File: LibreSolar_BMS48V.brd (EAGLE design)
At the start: 100 x 80 mm, 185 parts, among them IC1 BQ76940, Q1 ZXMP10A13F, Q10 DMN2004K, Q11 DMN2004K, Q12 DMN2004K, Q13 DMN2004K, Q14 DMN2004K, Q15 DMN2004K, Q16 DMN2004K, Q17 DMN2004K, Q18 DMN2004K, Q19 DMN2004K, Q2 FDMT80080DC, Q3 FDMT80080DC, Q4 2N7002ET1G, Q5 DMN2004K, Q6 DMN2004K, Q7 DMN2004K, Q8 DMN2004K, Q9 DMN2004K, U1 BQ76200, U2 LMR16006X, U3 ATMEGA328, Y1 8MHz

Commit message: Pinout of extension connector (LSX) changed
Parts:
- C10: value 4.7µ -> 1µ
- C19: value 470n -> 1µ
- LMX1: device resolut:LIBRE-CONNECTOR-10-2 -> LibreSolar:LIBRE-STD-EXT_SMALL
- R10: value 5m -> 1m
- moved LMX1 28.0 mm to (89.0, 48.0)
- moved N1 12.0 mm to (69.0, 40.0)
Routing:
- net D9: track 15.9 -> 44.4 mm
- net A0: track 50.8 -> 78.8 mm
- net A2: track 37.4 -> 65.4 mm
- net A1: track 27.8 -> 55.8 mm
- net D5: track 18.7 -> 46.7 mm
- net D3: track 33.9 -> 61.9 mm
- net SCL: track 61.6 -> 89.6 mm
- net SCK: track 68.2 -> 96.2 mm
- net SDA: track 67.7 -> 95.7 mm
- net 3.3V: track 172.8 -> 200.6 mm, vias 3 -> 4
- net SS: track 25.4 -> 52.0 mm
- net MOSI: track 40.8 -> 66.7 mm, vias 1 -> 2
- net RX: track 60.5 -> 85.8 mm
- net MISO: track 45.4 -> 68.6 mm, vias 1 -> 2
- net TX: track 66.4 -> 85.8 mm, vias 2 -> 3
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
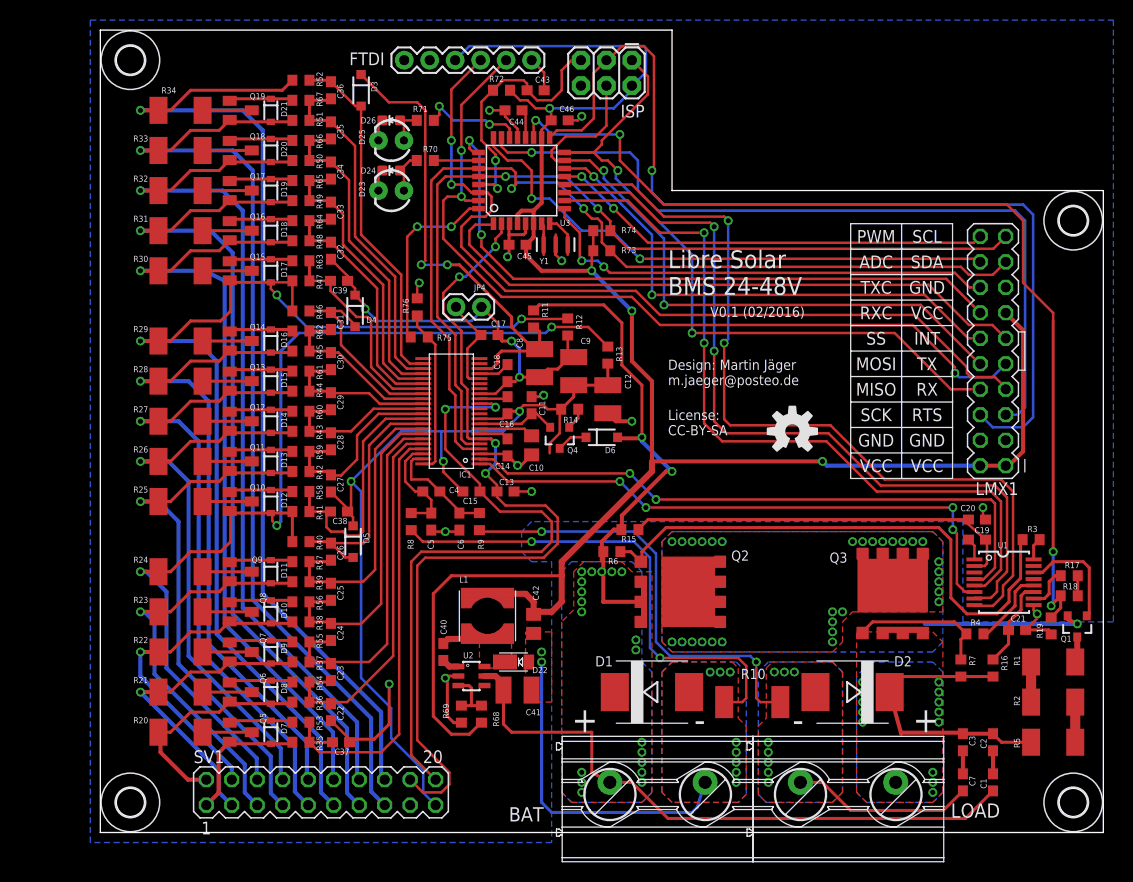
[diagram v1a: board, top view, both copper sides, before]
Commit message: Complete redesign with STM32F072 and external power part
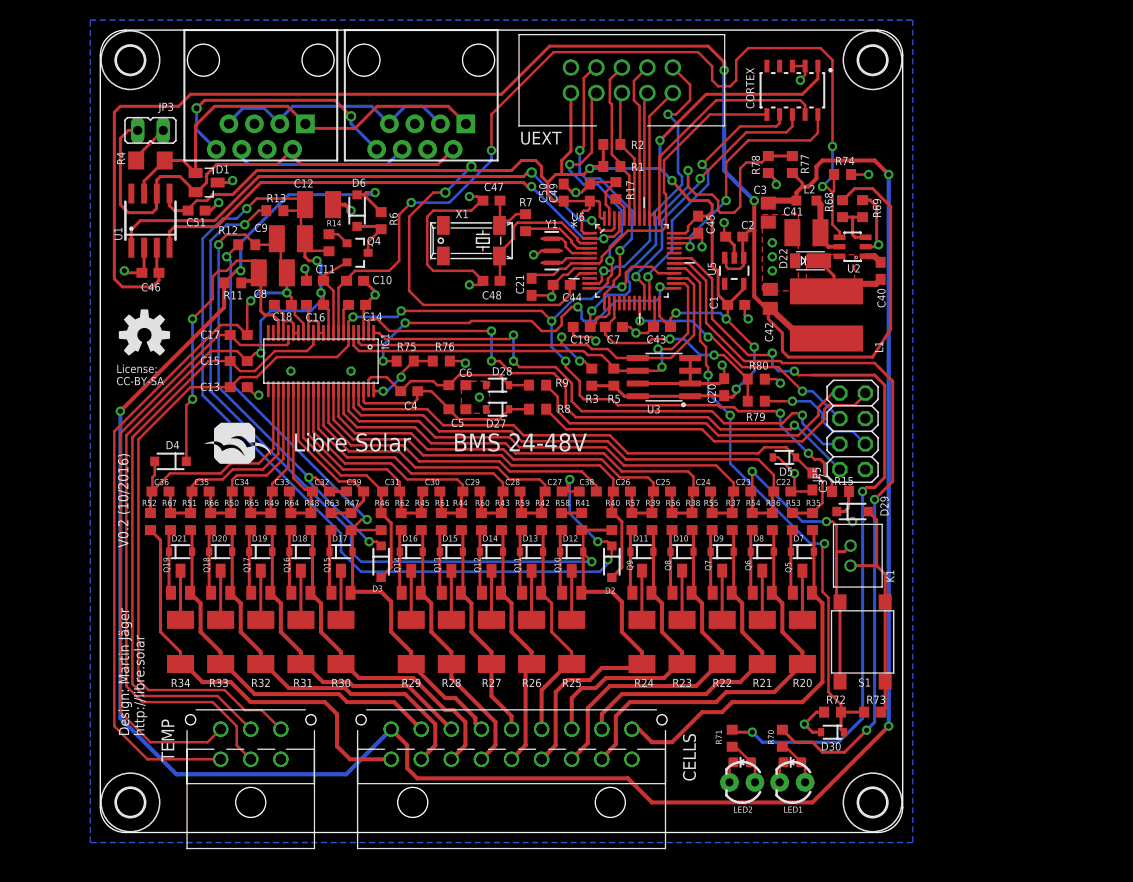
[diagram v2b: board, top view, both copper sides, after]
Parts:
- removed BAT, LOAD: MKDS_5/2-9,52, resolut:MKDS_5/2-952
- removed D23, D25: (no value), SparkFun-LED:LED3MM
- removed FTDI: FTDI Basic, SparkFun:1X06
- removed ISP: AVR_SPI_PRG_6PTH, SparkFun-Connectors:2X3
- removed JP4: M02PTH, SparkFun-Connectors:1X02
- removed LMX1: (no value), LibreSolar:LIBRE-STD-EXT_SMALL
- removed Q1: ZXMP10A13F, SparkFun-DiscreteSemi:SOT23-3
- removed Q2, Q3: FDMT80080DC, resolut:FDMT80080DC
- removed R10: 1m, rcl:R2512
- removed R16: 100, rcl:R0603
- removed R18: 100k, rcl:R0603
- removed R19: 10k, rcl:R0603
- removed SV1: (no value), con-lstb:MA10-2
- added C47, C48: 12.5p, rcl:C0603
- added C49, C51: 100n, rcl:C0603
- added C50: 2.2µ, rcl:C0603
- added CELLS: (no value), Wire_to_Board_Connectors_rev15d:66201821022
- added CORTEX: CORTEX_DEBUGSMD, LibreSolar:SAMTECH_FTSH-105-01
- added D27, D28, D30: 3.3V, SparkFun-DiscreteSemi:SOD-323
- added D29: 1N4148W, SparkFun-DiscreteSemi:SOD-123
- added JP1, JP2: RJ45, SparkFun-Connectors:RJ45-8
- added JP3: (no value), jumper:JP1
- added JP5: (no value), pinhead:2X04
- added K1: 62000211622, Wire_to_Board_Connectors_rev15d:62000211622
- added K4: 66200621122, Wire_to_Board_Connectors_rev15d:66200621122
- added K5: 66201821122, Wire_to_Board_Connectors_rev15d:66201821122
- added L2: 4.7uH, rcl:L2012C
- added LED1, LED2: (no value), SparkFun-LED:LED3MM
- added R77, R79: 100k, rcl:R0603
- added R78, R80: 5.6k, rcl:R0603
- added S1: (no value), EAGLE-TACT_SWITCHES-rev16e:430182050816
- added TEMP: 66200621022, Wire_to_Board_Connectors_rev15d:66200621022
- added U$1: LIBRESOLAR_LOGO, LibreSolar:LIBRESOLAR_LOGO
- added U5: MIC5225, SparkFun-PowerIC:SOT23-5
- added U6: STM32F072CB, LibreSolar:QFP50P900X900X160-48N
- added UEXT: UEXT, LibreSolar:UEXT
- added X1: ABS25-32.768KHZ-T, crystal:MM20SS
- C1: value 100n -> 2.2µ
- C10: device rcl:C0805 -> rcl:C0603
- C13, C15, C17: value 100n -> 4.7n
- C19: value 1µ -> 100n
- C2: value 100n -> 1µ
- C20, C21: value 10n -> 100n
- C3: value 100n -> 1µ; device rcl:C0603 -> rcl:C0805
- D1: value SMCJ75A -> PESD2CAN; device diode:SMC -> LibreSolar:SOT23
- D2: value ES3D-E3/57T -> 1N4148W; device diode:SMC -> SparkFun-DiscreteSemi:SOD-123
- D5: value 1N4148W -> 3.3V; device SparkFun-DiscreteSemi:SOD-123 -> SparkFun-DiscreteSemi:SOD-323
- IC1: device resolut:TSSOP44 -> LibreSolar:TSSOP44
- L1: value 100uH -> 47uH; device PowerMagnetics:WE-TPC_4818/4828 -> PowerMagnetics:WE-TPC_6823
- Q4: value 2N7002ET1G -> BSS123
- R1, R2, R5: value 33 -> 2.2k; device rcl:R2010 -> rcl:R0603
- R15: value 100 -> 5.6k
- R17: value 100k -> 10k
- R3: value 5 -> 2.2k
- R4: value 5 -> 120; device rcl:R0603 -> rcl:R1206
- R6: value 1M -> t.b.d.
- R68: value 33k -> 56k
- R7: value 1M -> 0R
- R72: value 10k -> 100k
- R73: value 2.2k -> 10k
- R74: value 2.2k -> 100k
- U1: value BQ76200 -> TJA1042T/3; device resolut:TSSOP16 -> LibreSolar:SOIC-8-N
- U3: value ATMEGA328 -> M24256-BW; device SparkFun:TQFP32-08 -> SparkFun-DigitalIC:SO08
- moved R4 94.8 mm to (5.00, 67.0)
- moved U1 92.3 mm to (5.00, 61.0), turned to 0 degrees
- moved D26 72.9 mm to (64.0, 7.00)
- moved D24 71.3 mm to (69.0, 7.00)
- moved R2 70.9 mm to (51.0, 68.6), turned to 180 degrees
- moved R72 70.2 mm to (73.0, 12.0)
- moved R71 68.8 mm to (63.0, 9.40), turned to 90 degrees
- moved R70 67.7 mm to (68.0, 9.40), turned to 90 degrees
- moved D1 67.5 mm to (10.6, 64.8), turned to 270 degrees
- moved R1 66.2 mm to (51.0, 66.4)
- moved N1 65.3 mm to (4.40, 49.6)
- moved R69 64.3 mm to (76.0, 62.2), turned to 270 degrees
- moved R20 62.6 mm to (70.0, 19.0), turned to 90 degrees
- moved R7 62.1 mm to (42.4, 60.8), turned to 90 degrees
- moved R68 61.9 mm to (74.0, 62.2), turned to 90 degrees
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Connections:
- removed net 3.3V: C42.1, C45.1, C46.1, FTDI.4, ISP.2, L1.2, LMX1.1, LMX1.13, LMX1.2, R68.2, R72.2, R73.2, R74.2, U3.18, U3.4, U3.6
- removed net A0: LMX1.5, U3.23
- removed net A1: LMX1.18, U3.24
- removed net A2: LMX1.14, U3.25
- removed net A3: R70.2, U3.26
- removed net A6: R18.1, R19.2, U3.19
- removed net A7: R71.2, U3.22
- removed net AREF: C44.1, U3.20
- removed net CHG: R3.1, U1.16
- removed net CHGDSG: Q1.2, Q2.D, Q3.D
- removed net D2: R75.2, U3.32
- removed net D3: LMX1.11, U3.1
- removed net D5: LMX1.16, U3.9
- removed net D6: U1.5, U3.10
- removed net D7: U1.7, U3.11
- removed net D8: U1.8, U3.12
- removed net D9: LMX1.20, U3.13
- removed net DSG: R4.1, U1.12
- removed net DTR: C43.1, FTDI.1
- removed net MISO: ISP.1, LMX1.8, U3.16
- removed net MOSI: ISP.4, LMX1.10, U3.15
- removed net N$26: C3.2, C7.1
- removed net N$38: C19.2, U1.1
- removed net N$47: C8.1, D3.C, IC1.20, R11.1
- removed net N$48: C1.2, C2.1
- removed net N$50: Q2.G, R3.2, R6.1
- removed net N$52: Q1.3, R1.1
- removed net N$54: R2.2, R5.2
- removed net N$55: R1.2, R2.1
- removed net N$6: Q3.G, R4.2, R7.1
- removed net PACK+: C2.2, C3.1, D2.C, LOAD.2, Q3.S, R16.2, R5.1, R7.2
- removed net PACK-: C7.2, D2.A, LOAD.1, R10.2, R9.1
- removed net PCHG: Q1.1, U1.14
- removed net RESET: C43.2, ISP.5, R72.1, U3.29
- removed net RX: FTDI.3, LMX1.7, U3.30
- removed net SCK: ISP.3, LMX1.6, U3.17
- removed net SCL: IC1.5, LMX1.19, R74.1, U3.28
- removed net SDA: IC1.4, LMX1.17, R73.1, U3.27
- removed net SS: LMX1.12, U3.14
- removed net TX: FTDI.2, LMX1.9, U3.31
- new net !CAN_EN!: U6.38
- new net !RESET: C21.1, CORTEX.10, U6.7
- new net +3V3: C1.1, C20.1, C43.1, C44.1, C45.1, C49.1, C50.1, C51.1, CORTEX.1, R1.2, R2.2, R3.2, R5.2, U1.5, U3.1, U3.8, U5.5, U6.1, U6.24, U6.36, U6.48, U6.9, UEXT.1
- new net +5V: C2.1, C42.1, C46.1, L1.2, R68.2, U1.3, U5.1, U5.3
- new net ALERT_IN: R75.2, U6.25
- new net BAT: C8.1, D4.C, IC1.20, R11.2
- new net BAT-: JP5.5
- new net BTN: D30.C, R72.2, R73.1, U6.29
- new net CAN_GND: JP1.3, JP1.7, JP2.3, JP2.7
- new net CAN_H: D1.1, JP1.1, JP2.1, R4.1, U1.7
- new net CAN_L: D1.2, JP1.2, JP2.2, JP3.2, U1.6
- new net CAN_RX: U1.4, U6.45
- new net CAN_SHLD: JP1.6, JP2.6
- new net CAN_STB: U1.8
- new net CAN_TX: U1.1, U6.46
- new net CAN_V+: JP1.8, JP2.8
- new net I2C1_SCL: R2.1, U6.42, UEXT.5
- new net I2C1_SDA: R1.1, U6.43, UEXT.6
- new net I2C2_SCL: IC1.5, R5.1, U3.6, U6.26
- new net I2C2_SDA: IC1.4, R3.1, U3.5, U6.27
- new net LED1: R70.2, U6.30
- new net LED2: R71.2, U6.31
- new net LOAD+: JP5.3, R79.2
- new net MCU_IN: D29.A, K1.1, R73.2, S1.2, S1.4
- new net N$57: R17.2, U6.44
- new net OSC_IN: U6.5, Y1.1
- new net OSC_OUT: U6.6, Y1.3
- new net PCHG_EN: JP5.6, U6.20
- new net PWR: C3.1, CELLS.18, D6.A, K5.18, L2.2, R11.1, R6.1, R77.2
- new net R_SENSE+: JP5.7, R8.1
- new net R_SENSE-: JP5.8, R9.1
- new net SPI1_MISO: U6.40, UEXT.7
- new net SPI1_MOSI: U6.41, UEXT.8
- new net SPI1_SCK: U6.39, UEXT.9
- new net SSEL: U6.11, UEXT.10
- new net SWCLK: CORTEX.4, U6.37
- new net SWDIO: CORTEX.2, U6.34
- new net USART2_RX: U6.13, UEXT.4
- new net USART2_TX: U6.12, UEXT.3
- new net USART3_RX: CORTEX.8, U6.22
- new net USART3_TX: CORTEX.6, U6.21
- new net USB_DM: U6.32
- new net USB_DP: U6.33
- new net V_BAT: C19.1, R77.1, R78.2, U6.14
- new net V_LOAD: C7.1, R79.1, R80.2, U6.15
- net BAT+: now also JP5.1; no longer BAT.1, C1.1, C41.1, D1.C, D6.A, Q2.S, R11.2, R15.2, R6.2, U2.5
- net C0: now also CELLS.10, K5.10; no longer SV1.1
- net C1: now also CELLS.2, K5.2; no longer SV1.2
- net C10: now also CELLS.15, K5.15; no longer SV1.11
- net C11: now also CELLS.7, K5.7; no longer SV1.12
- net C12: now also CELLS.16, K5.16; no longer SV1.13
- net C13: now also CELLS.8, K5.8; no longer SV1.14
- net C14: now also CELLS.17, K5.17; no longer SV1.15
- net C15: now also CELLS.9, K5.9; no longer SV1.16
- net C2: now also CELLS.11, K5.11; no longer SV1.3
- net C3: now also CELLS.3, K5.3; no longer SV1.4
- net C4: now also CELLS.12, K5.12; no longer SV1.5
- net C5: now also CELLS.4, K5.4; no longer SV1.6
- net C6: now also CELLS.13, K5.13; no longer SV1.7
- net C7: now also CELLS.5, K5.5; no longer SV1.8
- net C8: now also CELLS.14, K5.14; no longer SV1.9
- net C9: now also CELLS.6, K5.6; no longer SV1.10
- net CAP2: now also IC1.11, IC1.12
- net CAP3: now also IC1.16, IC1.17
- net CHG_EN: now also JP5.2; no longer U1.4
- net DSG_EN: now also JP5.4; no longer U1.6
- net GND: now also C1.2, C19.2, C2.2, C3.2, C37.2, C43.2, C47.2, C48.2, C49.2, C50.2, C51.2, C7.2, CELLS.1, CORTEX.3, CORTEX.5, D1.3, D27.A, D28.A, D30.A, D5.A, K4.1, K5.1, LED1.K, LED2.K, R17.1, R72.1, R74.1, R78.1, R80.1, TEMP.1, U1.2, U3.2, U3.4, U3.7, U5.2, U6.23, U6.35, U6.47, U6.8, UEXT.2; no longer BAT.2, C37.1, D1.A, D23.K, D25.K, FTDI.5, FTDI.6, ISP.6, LMX1.15, LMX1.3, LMX1.4, R10.1, R19.1, R8.1, SV1.17, U1.9, U3.21, U3.5
- net N$10: now also D29.C, R15.2; no longer U3.7, Y1.1
- net N$40: now also JP3.1, R4.2; no longer C19.1, C20.1, R15.1, U1.2
- net N$41: now also R7.1, U6.4; no longer C21.1, R16.1, U1.11
- net N$42: now also C47.1, R7.2, X1.1; no longer R17.2, U1.10
- net N$43: now also LED1.A; no longer D23.A
- net N$44: now also C48.1, U6.3, X1.4; no longer R17.1, R18.2
- net N$46: now also LED2.A; no longer D25.A
- net N$49: now also R6.2
- net N$9: now also C41.1, L2.1, U2.5; no longer U3.8, Y1.3
- net REGOUT: now also R74.2, U2.4
- net SRN: now also D28.C
- net SRP: now also D27.C
- net TS1: now also K4.4, R15.1, TEMP.4, U6.28; no longer SV1.18, U3.2
- net TS2: now also K4.5, TEMP.5; no longer SV1.20
- net TS3: now also K4.6, TEMP.6; no longer JP4.2
- net VC0: now also C37.1, D5.C; no longer C37.2
- net VC1: now also K1.2, S1.1, S1.3
- net VC10: now also D3.A; no longer D4.A
- net VC10X: now also D3.C, K4.3, TEMP.3; no longer D4.C, JP4.1
- net VC15: now also D4.A; no longer D3.A
- net VC5: now also D2.A; no longer D5.A
- net VC5X: now also D2.C, K4.2, TEMP.2; no longer D5.C, SV1.19
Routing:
- net PWR: track 0.00 -> 233.0 mm, vias 0 -> 5
- net 3.3V: track 200.6 -> 0.00 mm, vias 4 -> 0
- net +3V3: track 0.00 -> 199.3 mm, vias 0 -> 9
- net +5V: track 0.00 -> 168.0 mm, vias 0 -> 2
- net BAT+: track 113.8 -> 0.00 mm, vias 21 -> 0
- net A6: track 99.7 -> 0.00 mm, vias 4 -> 0
- net SCK: track 96.2 -> 0.00 mm, vias 1 -> 0
- net SDA: track 95.7 -> 0.00 mm, vias 2 -> 0
- net REGOUT: track 5.49 -> 95.3 mm, vias 0 -> 4
- net SCL: track 89.6 -> 0.00 mm, vias 2 -> 0
- net VC5X: track 92.9 -> 179.7 mm, vias 3 -> 7
- net TX: track 85.8 -> 0.00 mm, vias 3 -> 0
- net RX: track 85.8 -> 0.00 mm, vias 2 -> 0
- net VC10X: track 41.7 -> 126.6 mm, vias 3 -> 5
- net D8: track 83.7 -> 0.00 mm, vias 2 -> 0
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- removed copper zone on layer 1, net BAT+
- removed copper zone on layer 16, net BAT+
- removed copper zone on layer 1, net CHGDSG
- removed copper zone on layer 16, net CHGDSG
- removed copper zone on layer 1, net PACK+
- removed copper zone on layer 16, net PACK+
- removed copper zone on layer 1, net PACK-
- removed copper zone on layer 16, net PACK-
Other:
- board size 100 x 80 mm -> 80 x 80 mm
- board text added: "Design: Martin Jäger http://libre.solar"
- board text added: "V0.2 (10/2016)"
- board text removed: "+"
- board text removed: "-"
- board text removed: "Design: Martin Jäger m.jaeger@posteo.de"
- board text removed: "V0.1 (02/2016)"

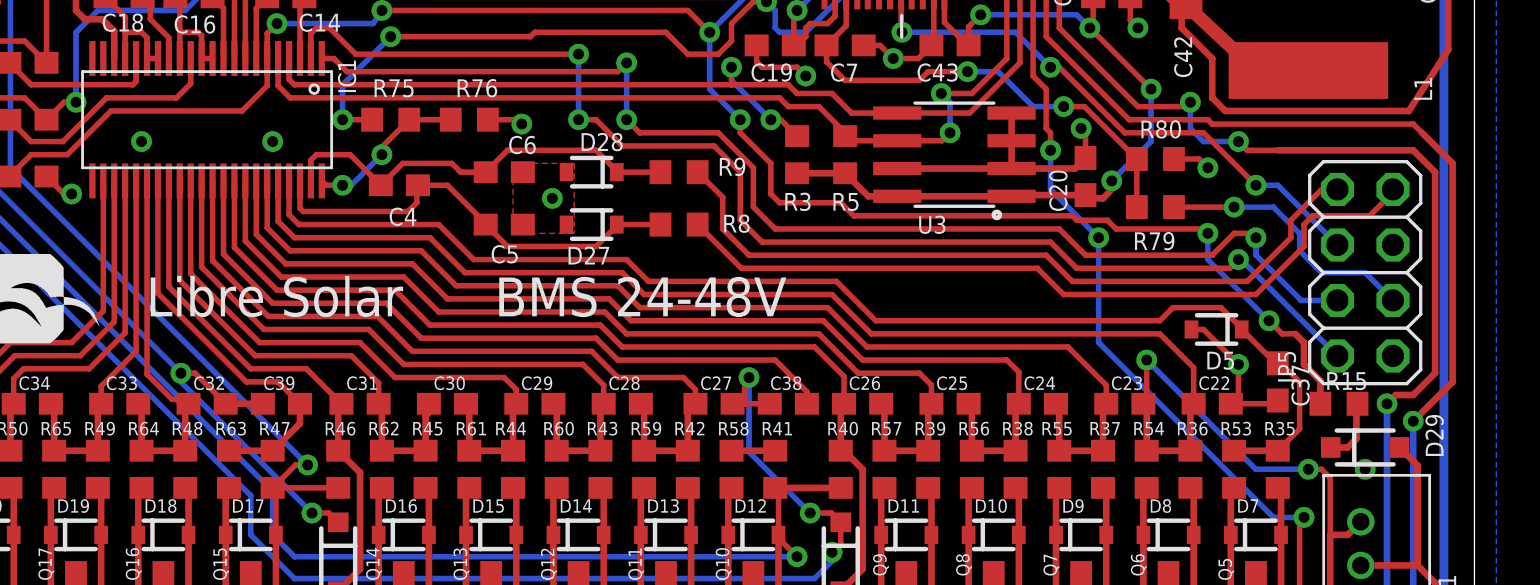
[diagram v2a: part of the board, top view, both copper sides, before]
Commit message: Uploaded image of assembled PCB
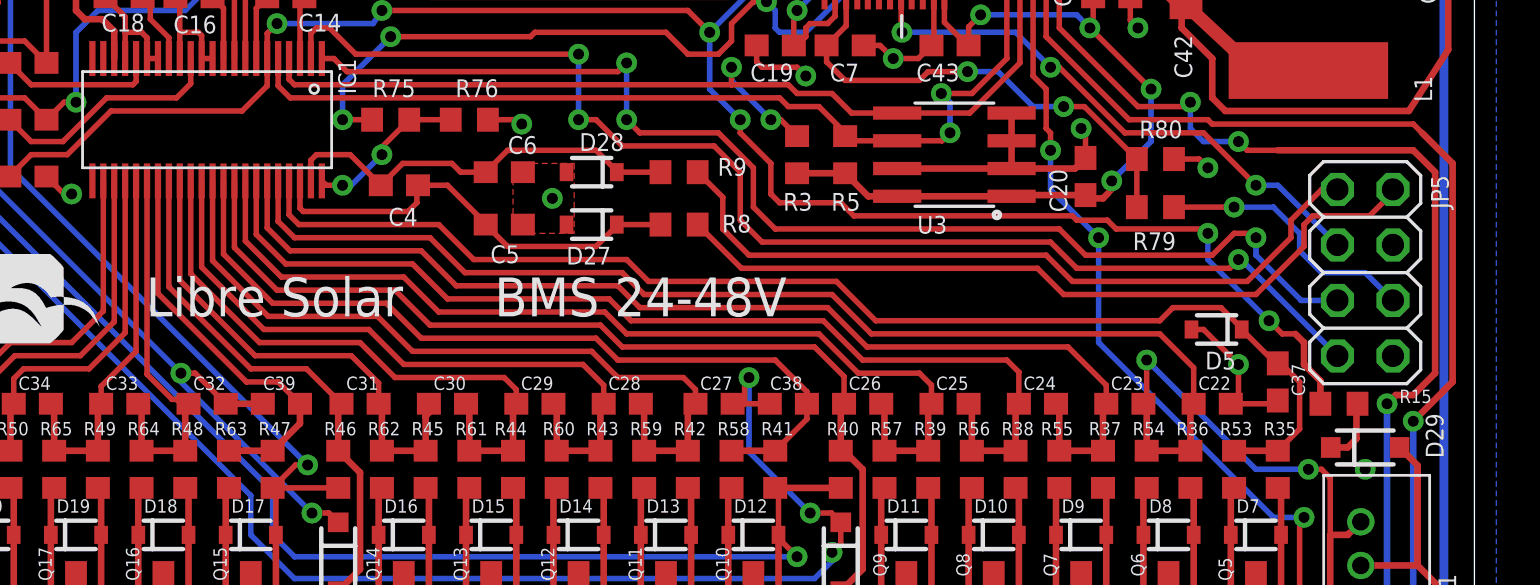
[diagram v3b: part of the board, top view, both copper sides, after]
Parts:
- C47, C48: value 12.5p -> 4.3p
- D1: value PESD2CAN -> NUP2105L
- X1: value ABS25-32.768KHZ-T -> ABS25-32.768KHZ-6
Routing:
- net VC5B: track 35.2 -> 38.0 mm
- net GND: vias 33 -> 31
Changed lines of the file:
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@@
 <?xml version="1.0" encoding="utf-8"?>
 <!DOCTYPE eagle SYSTEM "eagle.dtd">
-<eagle version="7.6.0">
+<eagle version="7.7.0">
 <drawing>
 <settings>
@@
 <layer number="29" name="tStop" color="7" fill="3" visible="no" active="yes"/>
 <layer number="30" name="bStop" color="7" fill="6" visible="no" active="yes"/>
-<layer number="31" name="tCream" color="7" fill="4" visible="no" active="yes"/>
+<layer number="31" name="tCream" color="7" fill="4" visible="yes" active="yes"/>
 <layer number="32" name="bCream" color="7" fill="5" visible="no" active="yes"/>
 <layer number="33" name="tFinish" color="6" fill="3" visible="no" active="yes"/>
@@
 <attribute name="MPN" value="0603B104K500CT" x="71" y="35" size="1.778" layer="27" rot="R270" display="off"/>
 <attribute name="MF" value="WALSIN" x="71" y="35" size="1.778" layer="27" rot="R270" display="off"/>
-<attribute name="NAME" x="71.635" y="35.835" size="0.8128" layer="25" font="vector" rot="R270"/>
+<attribute name="NAME" x="71.635" y="35.835" size="0.6096" layer="25" font="vector" rot="R270"/>
 <attribute name="VALUE" x="69.095" y="35.635" size="1.27" layer="27" rot="R270"/>
 </element>
@@
 <attribute name="VALUE" x="6.27" y="69.54" size="1.27" layer="27" rot="R180"/>
 </element>
-<element name="D1" library="LibreSolar" package="SOT23" value="PESD2CAN" x="10.6" y="64.8" smashed="yes" rot="R270">
+<element name="D1" library="LibreSolar" package="SOT23" value="NUP2105L" x="10.6" y="64.8" smashed="yes" rot="R270">
 <attribute name="MF" value="NXP" x="-55.4" y="151.8" size="1.778" layer="27" rot="R270" display="off"/>
 <attribute name="MPN" value="PESD2CAN" x="-55.4" y="151.8" size="1.778" layer="27" rot="R270" display="off"/>
@@
 <attribute name="VALUE" x="69" y="74" size="0.8128" layer="27" rot="R180" align="top-center"/>
 </element>
-<element name="X1" library="crystal" package="MM20SS" value="ABS25-32.768KHZ-T" x="37" y="59" smashed="yes" rot="R180">
+<element name="X1" library="crystal" package="MM20SS" value="ABS25-32.768KHZ-6" x="37" y="59" smashed="yes" rot="R180">
 <attribute name="MF" value="" x="112" y="151" size="1.778" layer="27" rot="R180" display="off"/>
 <attribute name="MPN" value="" x="112" y="151" size="1.778" layer="27" rot="R180" display="off"/>
@@
 <attribute name="VALUE" x="39.54" y="62.81" size="1.27" layer="27" ratio="10" rot="R180"/>
 </element>
-<element name="C47" library="rcl" package="C0603" value="12.5p" x="39" y="63" smashed="yes" rot="R180">
+<element name="C47" library="rcl" package="C0603" value="4.3p" x="39" y="63" smashed="yes" rot="R180">
 <attribute name="MF" value="MURATA" x="143" y="155" size="1.778" layer="27" rot="R180" display="off"/>
 <attribute name="MPN" value="GRM188R71H104KA93D" x="143" y="155" size="1.778" layer="27" rot="R180" display="off"/>
@@
 <attribute name="VALUE" x="39.635" y="64.905" size="1.27" layer="27" rot="R180"/>
 </element>
-<element name="C48" library="rcl" package="C0603" value="12.5p" x="39" y="55" smashed="yes" rot="R180">
+<element name="C48" library="rcl" package="C0603" value="4.3p" x="39" y="55" smashed="yes" rot="R180">
 <attribute name="MF" value="MURATA" x="150" y="152" size="1.778" layer="27" rot="R180" display="off"/>
 <attribute name="MPN" value="GRM188R71H104KA93D" x="150" y="152" size="1.778" layer="27" rot="R180" display="off"/>
@@
 <element name="Y1" library="Testing" package="RESONATOR-SMD-1:1" value="8MHz" x="45" y="58" smashed="yes" rot="R270">
 <attribute name="MF" value="MURATA" x="-85" y="203" size="1.778" layer="27" rot="R270" display="off"/>
-<attribute name="MPN" value="CSTCE8M00G55-R0" x="-85" y="203" size="1.778" layer="27" rot="R270" display="off"/>
-<attribute name="OC_FARNELL" value="2443270" x="-85" y="203" size="1.778" layer="27" rot="R270" display="off"/>
+<attribute name="MPN" value="CSTCE8M00G15C99-R0" x="-85" y="203" size="1.778" layer="27" rot="R270" display="off"/>
 <attribute name="NAME" x="44.384" y="60.27" size="0.8128" layer="25"/>
 <attribute name="VALUE" x="43.4125" y="58.9525" size="0.4064" layer="27" rot="R270"/>
@@
 </element>
 <element name="JP5" library="pinhead" package="2X04" value="" x="75" y="40" smashed="yes" rot="R90">
-<attribute name="NAME" x="71.825" y="34.92" size="0.8128" layer="25" ratio="10" rot="R90"/>
+<attribute name="NAME" x="78.825" y="42.92" size="0.8128" layer="25" ratio="10" rot="R90"/>
 <attribute name="VALUE" x="79.445" y="34.92" size="1.27" layer="27" rot="R90"/>
 </element>
@@
 <attribute name="MF" value="MULTICOMP" x="73.8" y="34" size="0.8128" layer="27" display="off"/>
 <attribute name="OC_FARNELL" value="2073348" x="73.8" y="34" size="0.8128" layer="27" display="off"/>
-<attribute name="NAME" x="73.165" y="34.635" size="0.8128" layer="25"/>
+<attribute name="NAME" x="76.565" y="34.035" size="0.6096" layer="25"/>
 <attribute name="VALUE" x="73.165" y="32.095" size="1.27" layer="27"/>
 </element>
@@
 <wire x1="36.8" y1="54.6" x2="38" y2="54.6" width="0.254" layer="1"/>
 <wire x1="38" y1="54.6" x2="38" y2="55" width="0.254" layer="1"/>
-<via x="19" y="46" extent="1-16" drill="0.5"/>
-<via x="25" y="46" extent="1-16" drill="0.5"/>
+<wire x1="19" y1="46" x2="19" y2="46" width="0" layer="19" extent="1-16"/>
+<wire x1="25" y1="46" x2="25" y2="46" width="0" layer="19" extent="1-16"/>
 <via x="67" y="57.4" extent="1-16" drill="0.5"/>
 <via x="67" y="58.8" extent="1-16" drill="0.5"/>
@@
 <wire x1="48" y1="36" x2="49.45" y2="34.55" width="0.254" layer="1"/>
 <wire x1="49.45" y1="34.55" x2="49.45" y2="34" width="0.254" layer="1"/>
-<wire x1="49.45" y1="34" x2="48" y2="31.85" width="0" layer="19" extent="1-1"/>
+<wire x1="48" y1="31.85" x2="49.45" y2="33.3" width="0.254" layer="1"/>
+<wire x1="49.45" y1="33.3" x2="49.45" y2="34" width="0.254" layer="1"/>
 </signal>
 <signal name="VC6">
